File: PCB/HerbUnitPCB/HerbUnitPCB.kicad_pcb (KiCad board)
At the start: 2 copper layers, 43 parts, among them J1 USB_C_Receptacle_USB2.0_16P, J2 Barrel_Jack_Switch_Pin3Ring, J3 Conn_01x03_Pin, J4 SD_Card_Device, J5 Screw_Terminal_01x02, J6 Conn_01x03_Pin, SW1 SW_Push, SW2 SW_Push, SW3 SW_Push, U1 USBLC6-2P6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

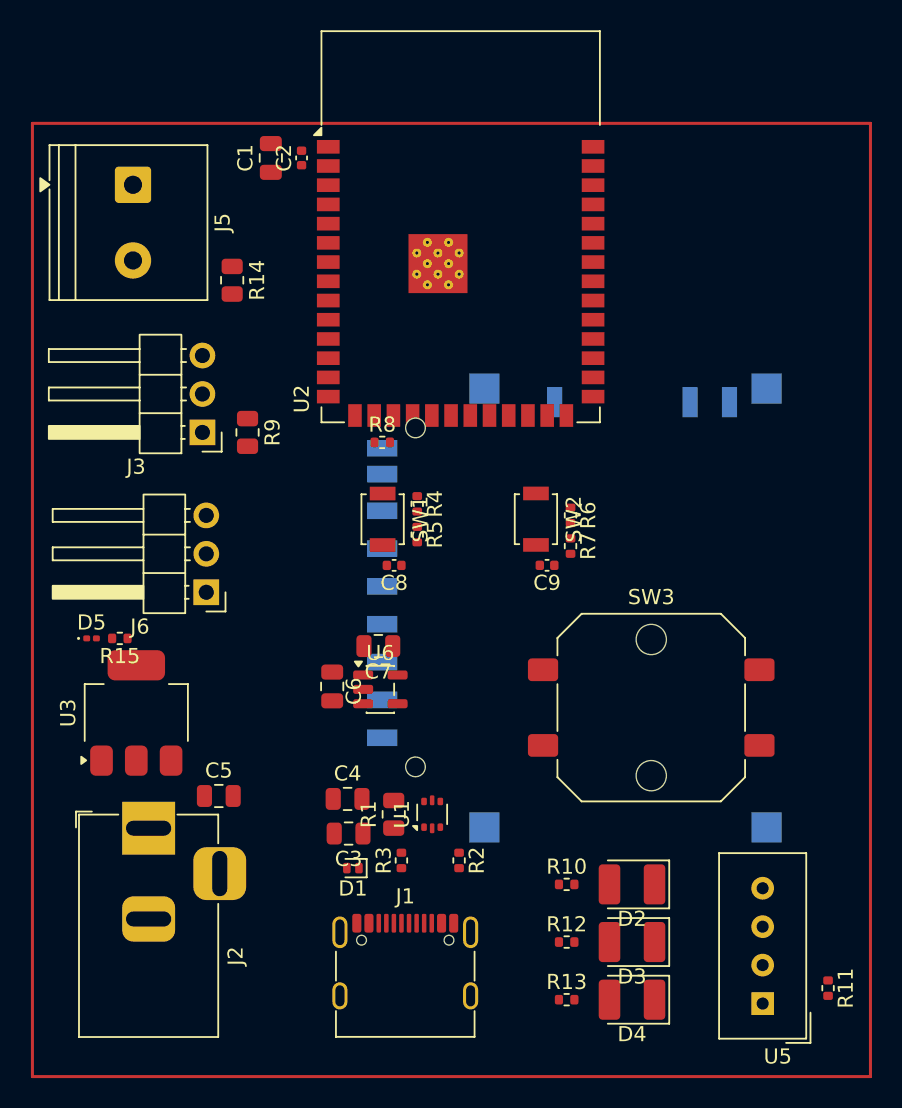
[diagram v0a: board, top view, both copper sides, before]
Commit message: Finished arrangement, fixed silkscreen
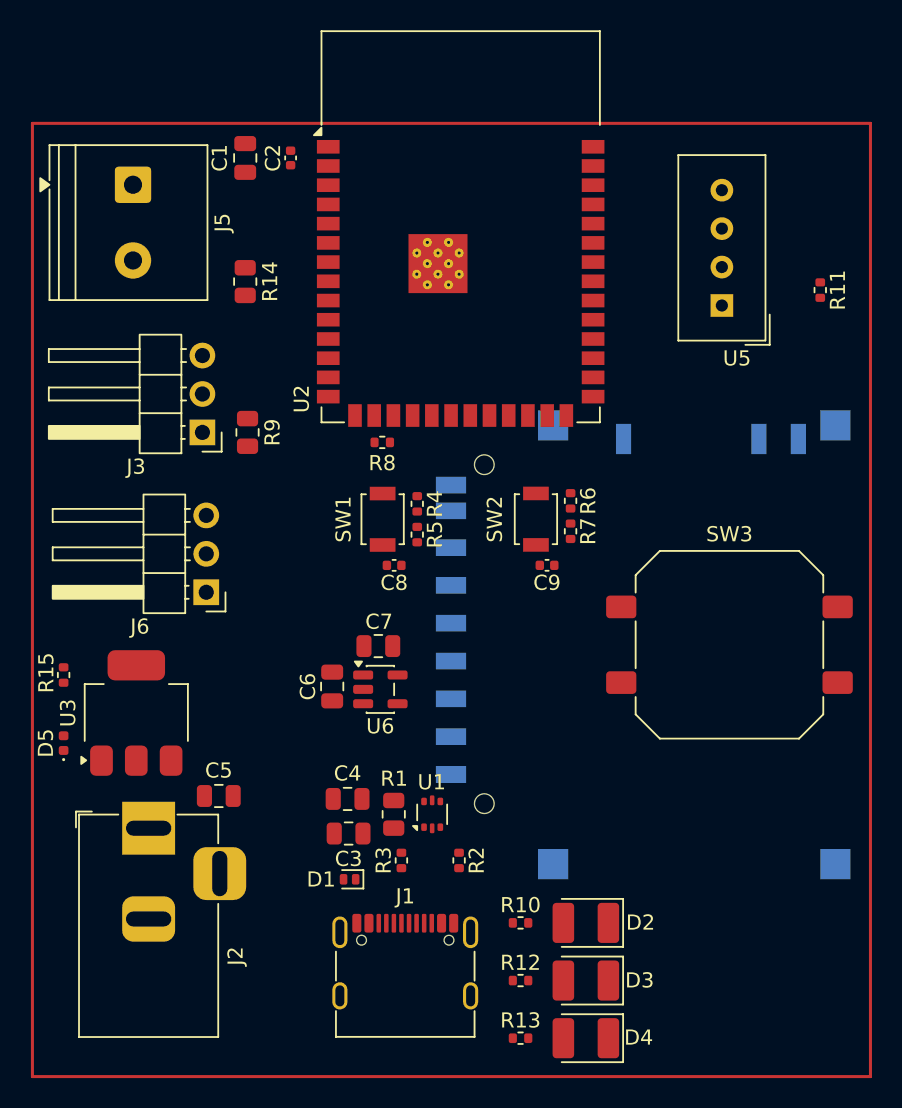
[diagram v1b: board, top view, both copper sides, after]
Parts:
- D5: footprint LED_SMD:LED_0201_0603Metric -> LED_SMD:LED_0402_1005Metric
- SW3: footprint Button_Switch_SMD:SW_Push_1P1T_NO_CK_PTS125Sx43PSMTR -> Button_Switch_SMD:SW_Push_1P1T_NO_CK_PTS125Sx43SMTR
- moved U5 46.2 mm to (184.5, 46.6)
- moved R11 46.1 mm to (191.0, 45.6)
- moved D5 7.16 mm to (141.0, 75.5), turned to 90 degrees
- moved SW3 6.63 mm to (185.0, 69.0)
- moved J4 5.16 mm to (181.6, 69.0)
- moved R15 4.43 mm to (141.0, 71.0), turned to -90 degrees
- moved D2 3.97 mm to (175.5, 87.4)
- moved D3 3.97 mm to (175.5, 91.2)
- moved D4 3.97 mm to (175.5, 95.0)
- moved R10 3.97 mm to (171.2, 87.4)
- moved R12 3.97 mm to (171.2, 91.2)
- moved R13 3.97 mm to (171.2, 95.0)
- moved C1 1.69 mm to (153.0, 36.8)
- moved R7 0.98 mm to (174.5, 61.5)
- moved R6 0.96 mm to (174.5, 59.5)
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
